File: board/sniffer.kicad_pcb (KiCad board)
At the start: 8 copper layers, 154 x 125 mm, 307 parts, among them J1 BARREL, J10 CONN_SFP_HOST, J11 SFP_CAGE, J12 PMOD_HOST, J13 CONN_SATA_DEVICE, J14 CONN_SATA_HOST, J15 CONN_LVDS_EXPANSION_HOST, J2 32K243-40ML5, J3 BEL_FUSE_0826-1G1T-23-F, J4 XILINX_JTAG, J5 32K243-40ML5, J6 32K243-40ML5, J7 32K243-40ML5, J8 CONN_SFF8087, J9 CONN_SFF8087, M1 SCREW_HOLE, M2 SCREW_HOLE, M3 SCREW_HOLE, M4 SCREW_HOLE, Q1 SSM6N58NU, U1 OKL-T_3-W12P-C, U10 KSZ9031RN, U11 74AVCH1T45, U12 74AVCH1T45, U13 74AVCH1T45, U14 74AVCH1T45, U15 W25Q128JV, U16 FPF2498, U17 FPF2498, U18 LP2996A, U2 LTC3374-QFN, U3 MYTNA1R84RELA2RA, U4 DDR3_SODIMM, U5 XC7K70T-2FBG484, U6 ECX2-LMV-7CN-156.250-TR, U7 ECX2-LMV-3CN-125.000-TR, U8 ECX2-LMV-3CN-125.000-TR, U9 SIT1602BC-72-18S-25.000000

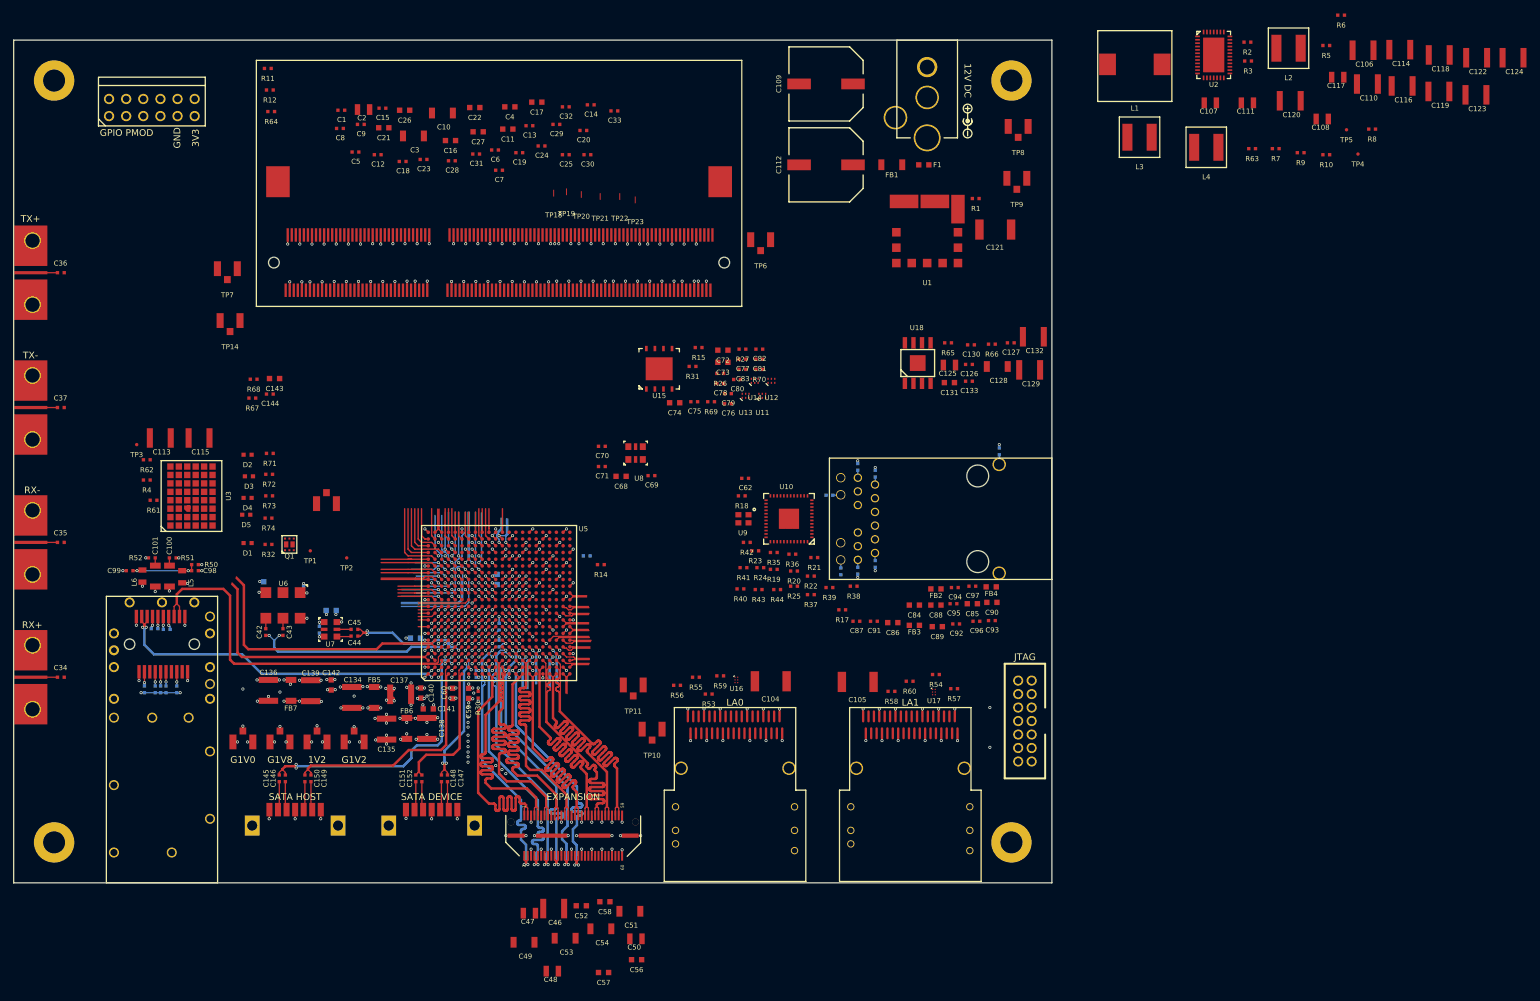
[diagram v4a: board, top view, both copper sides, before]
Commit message: Finished routing of south area of board including low speed SFP+ and LA connections. Started work on Ethernet.
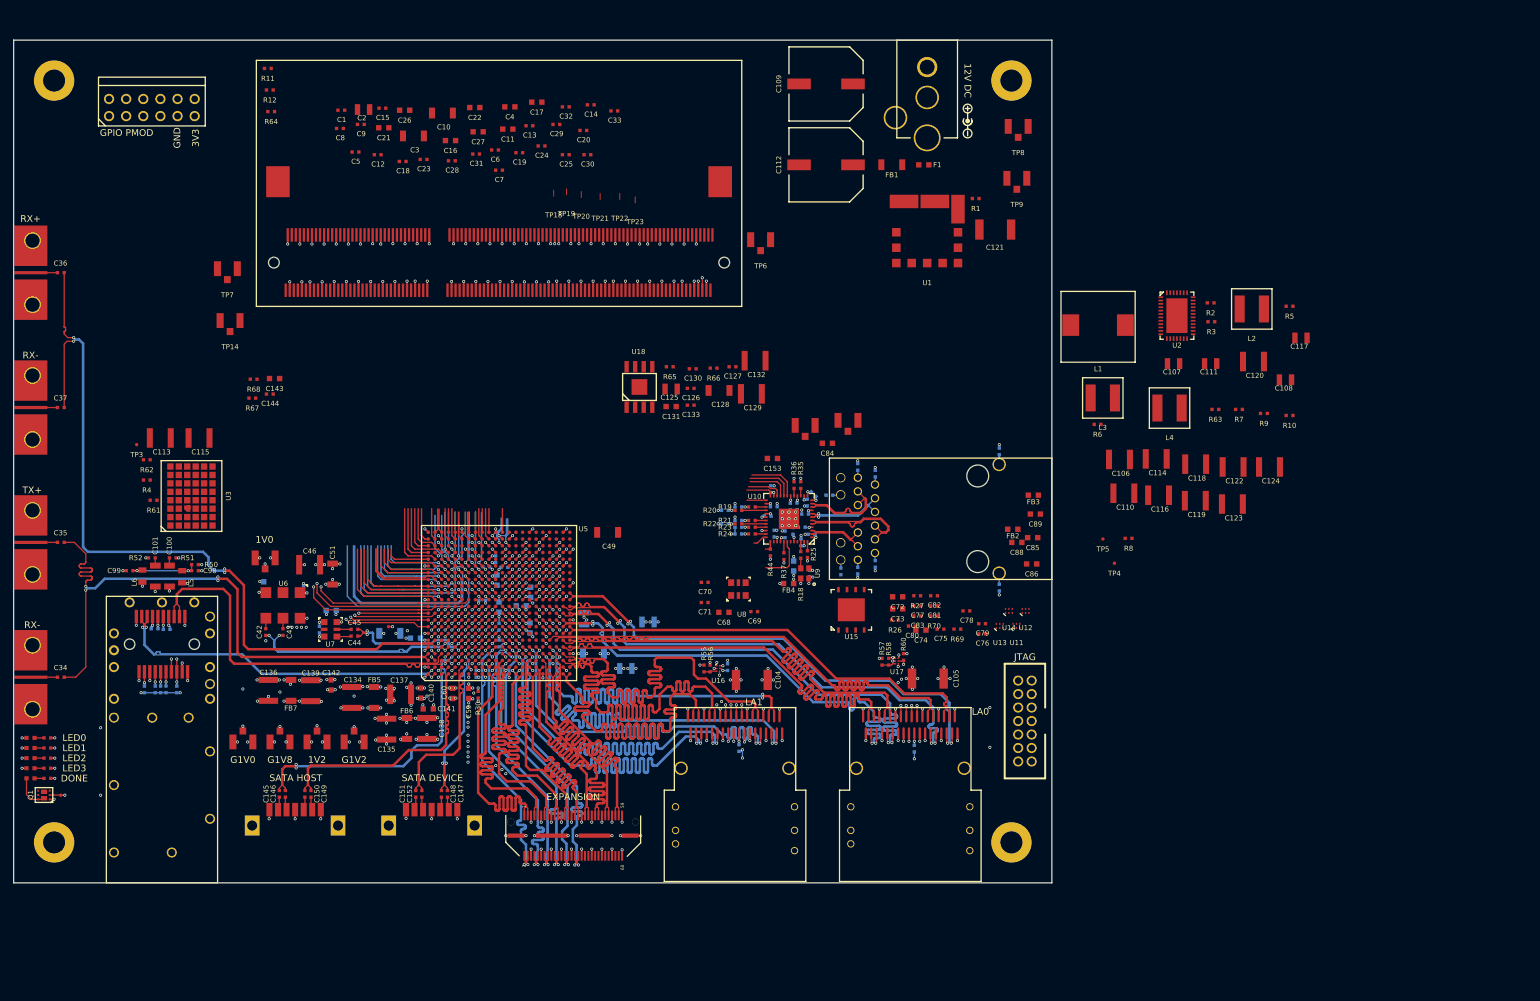
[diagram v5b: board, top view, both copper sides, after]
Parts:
- added C153: 4.7 uF, azonenberg_pcb:EIA_0603_CAP_NOSILK, F.Cu at (149.6, 95.0)
- added C154: 0.47 uF, azonenberg_pcb:EIA_0402_CAP_NOSILK, B.Cu at (152.2, 102.2)
- added C155: 0.47 uF, azonenberg_pcb:EIA_0402_CAP_NOSILK, B.Cu at (148.8, 103.6)
- added C156: 0.47 uF, azonenberg_pcb:EIA_0402_CAP_NOSILK, B.Cu at (154.7, 101.6)
- added C157: 0.47 uF, azonenberg_pcb:EIA_0402_CAP_NOSILK, B.Cu at (149.8, 102.2)
- added C158: 0.47 uF, azonenberg_pcb:EIA_0402_CAP_NOSILK, B.Cu at (149.8, 106.2)
- added C159: 0.47 uF, azonenberg_pcb:EIA_0402_CAP_NOSILK, B.Cu at (149.3, 99.6)
- C47, C48, C50, C52, C53, C54, C56, C57, C58, C62, C87, C90, C91, C92, C93, C94, C95, C96, C97, R14, R15, R17, R31, R38, R39, R40, R41, R42, R43, R53, R54, R59: moved to B.Cu
- U9: value SIT1602BC-72-18S-25.000000 -> ECS-2016MVQ-250-CN
- moved C110 70.6 mm to (201.7, 100.2)
- moved R6 70.6 mm to (197.8, 90.0)
- moved R8 70.6 mm to (202.4, 106.9)
- moved TP5 70.6 mm to (198.6, 107.0)
- moved C106 70.6 mm to (201.0, 95.2)
- moved C114 70.6 mm to (206.5, 95.1)
- moved C116 70.6 mm to (206.8, 100.5)
- moved C118 70.6 mm to (212.3, 95.9)
- moved C119 70.6 mm to (212.3, 101.3)
- moved C122 70.6 mm to (217.9, 96.3)
- moved C123 70.6 mm to (217.8, 101.8)
- moved TP4 70.6 mm to (200.3, 110.6)
- moved C124 70.6 mm to (223.3, 96.3)
- moved C51 66.7 mm to (84.3, 112.2), turned to 90 degrees
- moved C46 62.5 mm to (80.9, 110.8)
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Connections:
- C104 pad 1: /3.3V I/O/LA0_12V0 -> /3.3V I/O/LA1_12V0
- C105 pad 1: /3.3V I/O/LA1_12V0 -> /3.3V I/O/LA0_12V0
- C34 pad 1: /SERDES interfaces/GTX_TX3_P -> /SERDES interfaces/GTX_TX3_N
- C34 pad 2: /SERDES interfaces/GTX_TX3_AC_P -> /SERDES interfaces/GTX_TX3_AC_N
- C35 pad 1: /SERDES interfaces/GTX_TX3_N -> /SERDES interfaces/GTX_TX3_P
- C35 pad 2: /SERDES interfaces/GTX_TX3_AC_N -> /SERDES interfaces/GTX_TX3_AC_P
- C62 pad 1: /3V3 -> /1V8
- J6 pad 1: /SERDES interfaces/GTX_TX3_AC_P -> /SERDES interfaces/GTX_TX3_AC_N
- J7 pad 1: /SERDES interfaces/GTX_TX3_AC_N -> /SERDES interfaces/GTX_TX3_AC_P
- J8 pad A10: /3.3V I/O/LA0_PRESENCE_DETECT -> /3.3V I/O/LA1_PRESENCE_DETECT
- J8 pad A11: /3.3V I/O/LA0_12V0 -> /3.3V I/O/LA1_12V0
- J8 pad A13: /RGMII PHY/LA0_DQ6_P -> /Expansion connector/LA1_DQ6_P
- J8 pad A14: /RGMII PHY/LA0_DQ6_N -> /Expansion connector/LA1_DQ6_N
- J8 pad A16: /RGMII PHY/LA0_DQ7_P -> /Expansion connector/LA1_DQ7_P
- J8 pad A17: /RGMII PHY/LA0_DQ7_N -> /Expansion connector/LA1_DQ7_N
- J8 pad A2: /RGMII PHY/LA0_DQ4_P -> /Expansion connector/LA1_DQ4_P
- J8 pad A3: /RGMII PHY/LA0_DQ4_N -> /Expansion connector/LA1_DQ4_N
- J8 pad A5: /RGMII PHY/LA0_DQ5_P -> /Expansion connector/LA1_DQ5_P
- J8 pad A6: /RGMII PHY/LA0_DQ5_N -> /Expansion connector/LA1_DQ5_N
- J8 pad A8: /3.3V I/O/LA0_UART_RX -> /3.3V I/O/LA1_UART_RX
- J8 pad A9: /3.3V I/O/LA0_UART_TX -> /3.3V I/O/LA1_UART_TX
- J8 pad B10: /3.3V I/O/LA0_12V0 -> /3.3V I/O/LA1_12V0
- J8 pad B11: /3.3V I/O/LA0_12V0 -> /3.3V I/O/LA1_12V0
- J8 pad B13: /RGMII PHY/LA0_DQ2_P -> /Expansion connector/LA1_DQ2_P
- J8 pad B14: /RGMII PHY/LA0_DQ2_N -> /Expansion connector/LA1_DQ2_N
- J8 pad B16: /RGMII PHY/LA0_DQ3_P -> /Expansion connector/LA1_DQ3_P
- J8 pad B17: /RGMII PHY/LA0_DQ3_N -> /Expansion connector/LA1_DQ3_N
- J8 pad B2: /RGMII PHY/LA0_DQ0_P -> /Expansion connector/LA1_DQ0_P
- J8 pad B3: /RGMII PHY/LA0_DQ0_N -> /Expansion connector/LA1_DQ0_N
- J8 pad B5: /RGMII PHY/LA0_DQ1_P -> /Expansion connector/LA1_DQ1_P
- J8 pad B6: /RGMII PHY/LA0_DQ1_N -> /Expansion connector/LA1_DQ1_N
- J8 pad B8: /3.3V I/O/LA0_12V0 -> /3.3V I/O/LA1_12V0
- J8 pad B9: /3.3V I/O/LA0_12V0 -> /3.3V I/O/LA1_12V0
- J9 pad A10: /3.3V I/O/LA1_PRESENCE_DETECT -> /3.3V I/O/LA0_PRESENCE_DETECT
- J9 pad A11: /3.3V I/O/LA1_12V0 -> /3.3V I/O/LA0_12V0
- J9 pad A13: /Expansion connector/LA1_DQ6_P -> /RGMII PHY/LA0_DQ6_P
- J9 pad A14: /Expansion connector/LA1_DQ6_N -> /RGMII PHY/LA0_DQ6_N
- J9 pad A16: /Expansion connector/LA1_DQ7_P -> /RGMII PHY/LA0_DQ7_P
- J9 pad A17: /Expansion connector/LA1_DQ7_N -> /RGMII PHY/LA0_DQ7_N
- J9 pad A2: /Expansion connector/LA1_DQ4_P -> /RGMII PHY/LA0_DQ4_P
- J9 pad A3: /Expansion connector/LA1_DQ4_N -> /RGMII PHY/LA0_DQ4_N
- J9 pad A5: /Expansion connector/LA1_DQ5_P -> /RGMII PHY/LA0_DQ5_P
- J9 pad A6: /Expansion connector/LA1_DQ5_N -> /RGMII PHY/LA0_DQ5_N
- J9 pad A8: /3.3V I/O/LA1_UART_RX -> /3.3V I/O/LA0_UART_RX
- J9 pad A9: /3.3V I/O/LA1_UART_TX -> /3.3V I/O/LA0_UART_TX
- J9 pad B10: /3.3V I/O/LA1_12V0 -> /3.3V I/O/LA0_12V0
- J9 pad B11: /3.3V I/O/LA1_12V0 -> /3.3V I/O/LA0_12V0
- J9 pad B13: /Expansion connector/LA1_DQ2_P -> /RGMII PHY/LA0_DQ2_P
- J9 pad B14: /Expansion connector/LA1_DQ2_N -> /RGMII PHY/LA0_DQ2_N
- J9 pad B16: /Expansion connector/LA1_DQ3_P -> /RGMII PHY/LA0_DQ3_P
- J9 pad B17: /Expansion connector/LA1_DQ3_N -> /RGMII PHY/LA0_DQ3_N
- J9 pad B2: /Expansion connector/LA1_DQ0_P -> /RGMII PHY/LA0_DQ0_P
- J9 pad B3: /Expansion connector/LA1_DQ0_N -> /RGMII PHY/LA0_DQ0_N
- J9 pad B5: /Expansion connector/LA1_DQ1_P -> /RGMII PHY/LA0_DQ1_P
- J9 pad B6: /Expansion connector/LA1_DQ1_N -> /RGMII PHY/LA0_DQ1_N
- J9 pad B8: /3.3V I/O/LA1_12V0 -> /3.3V I/O/LA0_12V0
- J9 pad B9: /3.3V I/O/LA1_12V0 -> /3.3V I/O/LA0_12V0
- R53 pad 1: /3.3V I/O/LA0_PRESENCE_DETECT -> /3.3V I/O/LA1_PRESENCE_DETECT
- R54 pad 1: /3.3V I/O/LA1_PRESENCE_DETECT -> /3.3V I/O/LA0_PRESENCE_DETECT
- R59 pad 2: /3.3V I/O/LA0_12V0_EN -> /3.3V I/O/LA1_12V0_EN
- R60 pad 2: /3.3V I/O/LA1_12V0_EN -> /3.3V I/O/LA0_12V0_EN
- U16 pad B1: /3.3V I/O/LA0_12V0 -> /3.3V I/O/LA1_12V0
- U16 pad B2: /3.3V I/O/LA0_12V0_EN -> /3.3V I/O/LA1_12V0_EN
- U16 pad C2: /3.3V I/O/LA0_12V0_FAULT -> /3.3V I/O/LA1_12V0_FAULT
- U17 pad B1: /3.3V I/O/LA1_12V0 -> /3.3V I/O/LA0_12V0
- U17 pad B2: /3.3V I/O/LA1_12V0_EN -> /3.3V I/O/LA0_12V0_EN
- U17 pad C2: /3.3V I/O/LA1_12V0_FAULT -> /3.3V I/O/LA0_12V0_FAULT
- U5 pad A10: /3.3V I/O/ETH_LED1_P -> /3.3V I/O/LED3
- U5 pad A11: /3.3V I/O/PMOD_DQ1 -> /3.3V I/O/PMOD_DQ3
- U5 pad A9: /3.3V I/O/LED3 -> /3.3V I/O/LED1
- U5 pad AA1: /Expansion connector/LA1_DQ5_P -> /Expansion connector/LA1_DQ0_P
- U5 pad AA10: /RGMII PHY/LA0_DQ7_P -> /RGMII PHY/LA0_DQ5_P
- U5 pad AA11: /RGMII PHY/LA0_DQ2_P -> /RGMII PHY/LA0_DQ6_P
- U5 pad AA3: /Expansion connector/LA1_DQ6_P -> /Expansion connector/LA1_DQ1_N
- U5 pad AA4: /Expansion connector/LA1_DQ7_P -> /Expansion connector/LA1_DQ2_N
- U5 pad AA5: /RGMII PHY/LA0_DQ3_P -> /RGMII PHY/LA0_DQ0_P
- U5 pad AA6: /RGMII PHY/LA0_DQ4_P -> /RGMII PHY/LA0_DQ1_P
- U5 pad AA8: /RGMII PHY/LA0_DQ0_N -> /RGMII PHY/LA0_DQ4_P
- U5 pad AA9: /RGMII PHY/LA0_DQ0_P -> /RGMII PHY/LA0_DQ4_N
- U5 pad AB1: /Expansion connector/LA1_DQ5_N -> /Expansion connector/LA1_DQ0_N
- U5 pad AB10: /RGMII PHY/LA0_DQ7_N -> /RGMII PHY/LA0_DQ5_N
- U5 pad AB11: /RGMII PHY/LA0_DQ2_N -> /RGMII PHY/LA0_DQ6_N
- U5 pad AB12: /RGMII PHY/LA0_DQ1_N -> /RGMII PHY/LA0_DQ7_P
- U5 pad AB13: /RGMII PHY/LA0_DQ1_P -> /RGMII PHY/LA0_DQ7_N
- U5 pad AB2: /Expansion connector/LA1_DQ6_N -> /Expansion connector/LA1_DQ1_P
- U5 pad AB3: /Expansion connector/LA1_DQ7_N -> /Expansion connector/LA1_DQ2_P
- U5 pad AB5: /RGMII PHY/LA0_DQ3_N -> /RGMII PHY/LA0_DQ0_N
- U5 pad AB6: /RGMII PHY/LA0_DQ4_N -> /RGMII PHY/LA0_DQ1_N
- U5 pad AB7: /RGMII PHY/LA0_DQ5_N -> /RGMII PHY/LA0_DQ3_P
- U5 pad AB8: /RGMII PHY/LA0_DQ5_P -> /RGMII PHY/LA0_DQ3_N
- U5 pad B10: /3.3V I/O/PMOD_DQ7 -> /3.3V I/O/LED2
- U5 pad B11: /3.3V I/O/LED1 -> /3.3V I/O/PMOD_DQ6
- U5 pad B8: /3.3V I/O/LA1_12V0_FAULT -> /3.3V I/O/LA1_UART_RX
- U5 pad C10: /3.3V I/O/LA1_PRESENCE_DETECT -> /3.3V I/O/LA1_UART_TX
- U5 pad C8: /3.3V I/O/LA1_UART_TX -> /3.3V I/O/LA1_PRESENCE_DETECT
- U5 pad C9: /3.3V I/O/LA0_12V0_EN -> /3.3V I/O/LA1_12V0_EN
- U5 pad D10: /3.3V I/O/PMOD_DQ2 -> /3.3V I/O/PMOD_DQ5
- U5 pad D9: /3.3V I/O/LA1_12V0_EN -> /3.3V I/O/LA1_12V0_FAULT
- U5 pad E11: /3.3V I/O/SFP_TX_DISABLE -> /3.3V I/O/SFP_RX_LOS
- U5 pad E12: /3.3V I/O/SFP_TX_FAULT -> /3.3V I/O/SFP_MOD_ABS
- U5 pad E13: /SERDES interfaces/SFP_I2C_SCL -> /3.3V I/O/SFP_TX_DISABLE
- U5 pad E8: /3.3V I/O/LA1_UART_RX -> /3.3V I/O/LA0_UART_TX
- U5 pad E9: /3.3V I/O/LA0_12V0_FAULT -> /3.3V I/O/LA0_UART_RX
- U5 pad F10: /3.3V I/O/PMOD_DQ0 -> /3.3V I/O/PMOD_DQ1
- U5 pad F11: /3.3V I/O/SFP_RX_LOS -> /3.3V I/O/SFP_RS0
- U5 pad F13: /SERDES interfaces/SFP_I2C_SDA -> /3.3V I/O/SFP_TX_FAULT
- U5 pad F8: /3.3V I/O/LA0_UART_RX -> /3.3V I/O/LA0_12V0_EN
- U5 pad F9: /3.3V I/O/LA0_UART_TX -> /3.3V I/O/LA0_PRESENCE_DETECT
- U5 pad G11: /3.3V I/O/PMOD_DQ3 -> /3.3V I/O/PMOD_DQ2
- U5 pad G12: /3.3V I/O/PMOD_DQ6 -> /3.3V I/O/PMOD_DQ7
- U5 pad G13: /3.3V I/O/SFP_MOD_ABS -> /SERDES interfaces/SFP_I2C_SDA
- U5 pad G8: /3.3V I/O/LA0_PRESENCE_DETECT -> /3.3V I/O/LA0_12V0_FAULT
- U5 pad H10: /3.3V I/O/LED2 -> /3.3V I/O/PMOD_DQ0
- U5 pad H12: /3.3V I/O/PMOD_DQ5 -> (no net)
- U5 pad H13: /3.3V I/O/SFP_RS0 -> /SERDES interfaces/SFP_I2C_SCL
- U5 pad H8: (no net) -> /3.3V I/O/ETH_LED1_P
- U5 pad T13: /RGMII PHY/ETH_LED2_N_1V8 -> (no net)
- U5 pad T4: /Expansion connector/LA1_DQ3_P -> /Expansion connector/LA1_DQ5_P
- U5 pad T5: /Expansion connector/LA1_DQ1_P -> /Expansion connector/LA1_DQ6_P
- U5 pad T8: /RGMII PHY/RGMII_TX_CLK -> (no net)
- U5 pad T9: /RGMII PHY/RGMII_TXD3 -> (no net)
- U5 pad U3: /Expansion connector/LA1_DQ3_N -> /Expansion connector/LA1_DQ5_N
- U5 pad U5: /Expansion connector/LA1_DQ1_N -> /Expansion connector/LA1_DQ6_N
- U5 pad V4: /Expansion connector/LA1_DQ0_P -> /Expansion connector/LA1_DQ7_P
- U5 pad V7: (no net) -> /RGMII PHY/RGMII_TX_CLK
- U5 pad V8: (no net) -> /RGMII PHY/RGMII_TXD3
- U5 pad W10: (no net) -> /RGMII PHY/ETH_LED2_N_1V8
- U5 pad W4: /Expansion connector/LA1_DQ0_N -> /Expansion connector/LA1_DQ7_N
- U5 pad W5: /Expansion connector/LA1_DQ2_P -> /Expansion connector/LA1_DQ3_P
- U5 pad W6: /RGMII PHY/LA0_DQ6_P -> /RGMII PHY/LA0_DQ2_N
- U5 pad Y4: /Expansion connector/LA1_DQ2_N -> /Expansion connector/LA1_DQ3_N
- U5 pad Y6: /RGMII PHY/LA0_DQ6_N -> /RGMII PHY/LA0_DQ2_P
- U9 pad 1: /3V3 -> /1V8
- U9 pad 4: /3V3 -> /1V8
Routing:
- net /3V3: track 176.0 -> 465.0 mm, vias 13 -> 19
- net /12V0: track 0.00 -> 264.5 mm, vias 0 -> 4
- net /GND: track 1644.0 -> 1850.2 mm, vias 260 -> 318
- net /1V8: track 137.3 -> 292.1 mm, vias 31 -> 48
- net /3.3V I/O/PMOD_DQ4: track 0.71 -> 118.3 mm, vias 1 -> 2
- net /3.3V I/O/PMOD_DQ0: track 0.71 -> 118.2 mm, vias 1 -> 2
- net /3.3V I/O/PMOD_DQ5: track 0.71 -> 112.7 mm, vias 1 -> 2
- net /3.3V I/O/PMOD_DQ1: track 1.50 -> 112.7 mm, vias 0 -> 2
- net /3.3V I/O/PMOD_DQ2: track 0.71 -> 111.4 mm, vias 1 -> 2
- net /3.3V I/O/PMOD_DQ7: track 2.71 -> 108.4 mm, vias 0 -> 1
- net /3.3V I/O/PMOD_DQ3: track 0.71 -> 99.4 mm
- net /3.3V I/O/PMOD_DQ6: track 7.71 -> 104.6 mm, vias 0 -> 1
- net /FPGA support/FPGA_DONE: track 16.2 -> 91.1 mm, vias 1 -> 5
- net /3.3V I/O/LED2: track 0.71 -> 74.0 mm, vias 1 -> 2
- net /3.3V I/O/LED3: track 1.50 -> 73.9 mm, vias 0 -> 2
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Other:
- board text added: "1V0"
- board text added: "DONE"
- board text added: "LED0"
- board text added: "LED1"
- board text added: "LED2"
- board text added: "LED3"
- board text removed: "TX-"

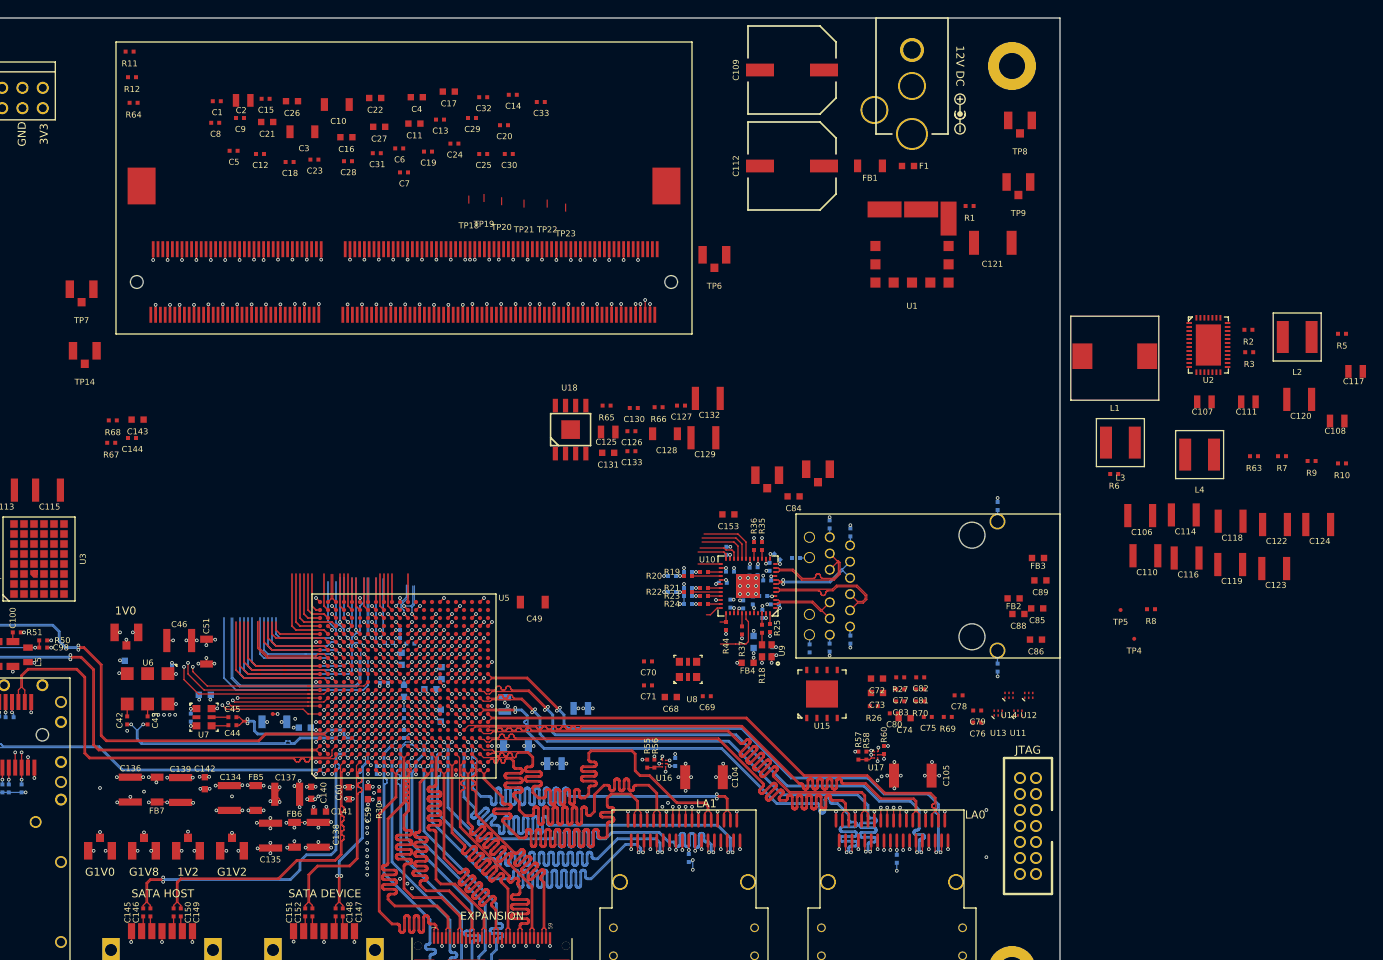
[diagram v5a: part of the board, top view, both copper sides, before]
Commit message: Finished routing almost everything except DDR.
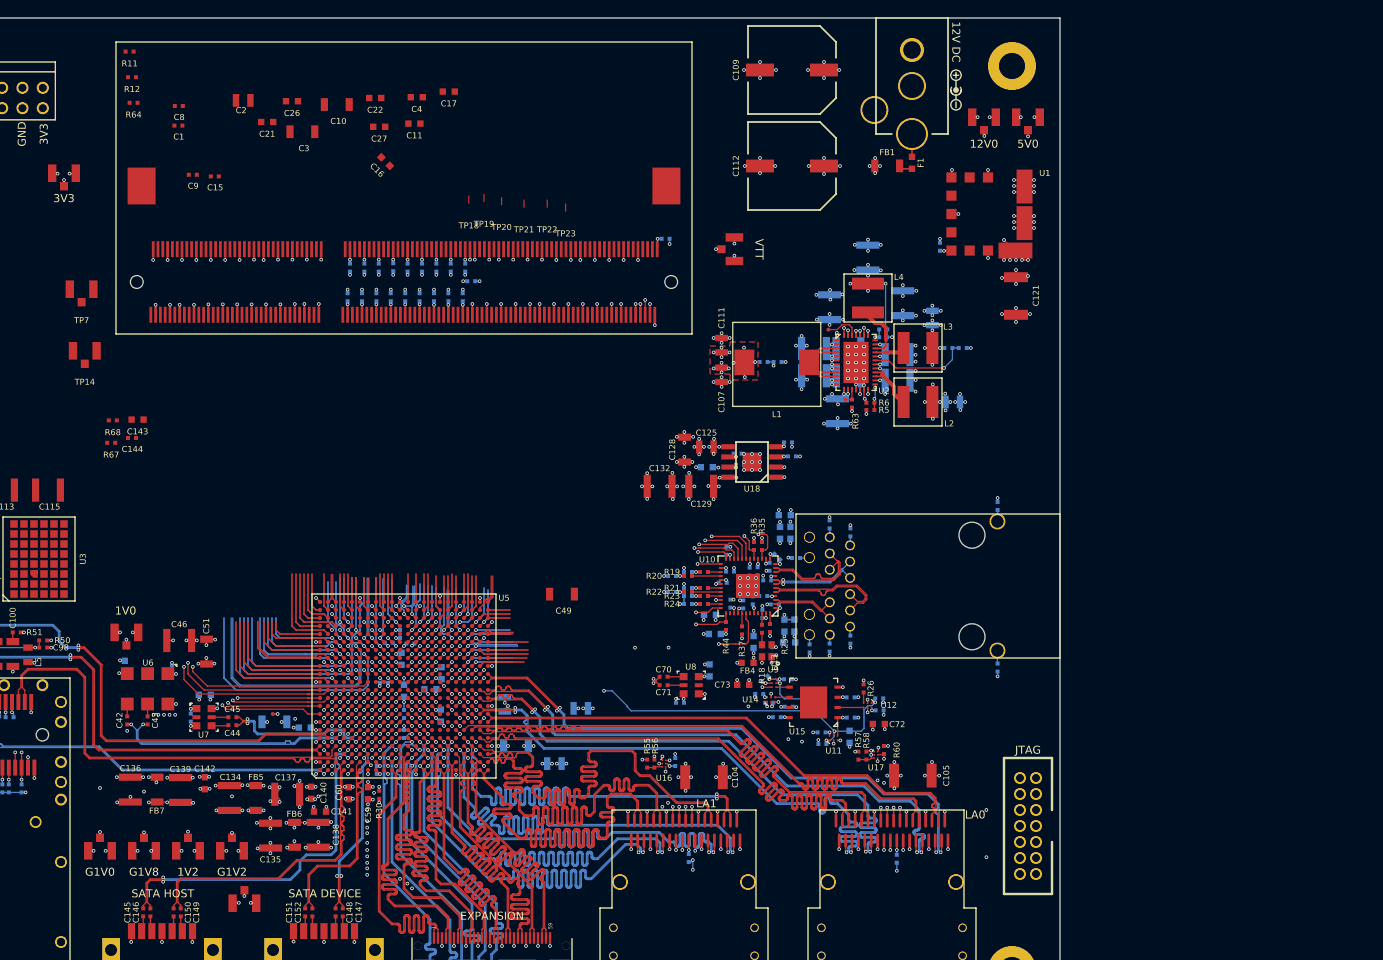
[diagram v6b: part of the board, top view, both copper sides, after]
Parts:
- C106, C108, C110, C114, C116, C117, C118, C119, C12, C120, C122, C123, C124, C126, C127, C13, C130, C131, C133, C14, C153, C18, C19, C20, C23, C24, C25, C28, C29, C30, C31, C32, C33, C5, C6, C68, C69, C7, C74, C75, C76, C77, C78, C79, C80, C81, C82, C83, C84, C85, C86, C88, C89, FB2, FB3, R1, R10, R2, R27, R3, R65, R66, R69, R7, R70, R8, R9: moved to B.Cu
- moved TP10 101.3 mm to (66.5, 52.5)
- moved TP11 84.3 mm to (89.0, 143.6), turned to 180 degrees
- moved C124 66.8 mm to (162.2, 69.2), turned to 90 degrees
- moved C111 66.2 mm to (148.7, 73.9), turned to 90 degrees
- moved R2 60.7 mm to (153.9, 76.0)
- moved C107 60.4 mm to (148.7, 77.6), turned to 270 degrees
- moved R5 59.7 mm to (167.3, 82.0)
- moved R10 59.5 mm to (168.9, 72.9)
- moved R3 59.0 mm to (155.7, 76.0)
- moved C123 58.0 mm to (163.2, 82.2), turned to 90 degrees
- moved C120 56.7 mm to (167.0, 63.0), turned to 90 degrees
- moved R9 56.0 mm to (168.9, 71.9), turned to 180 degrees
- moved TP4 54.4 mm to (162.1, 72.0)
- moved C117 53.3 mm to (175.1, 70.5), turned to 90 degrees
- moved C119 52.4 mm to (171.3, 68.7), turned to 90 degrees
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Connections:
- net Net-(R10-Pad1) renamed /Power Supply/3V3_FB
- net Net-(R7-Pad2) renamed /Power Supply/1V8_FB
- R5 pad 2: /Power Supply/1V35_FB -> /Power Supply/1V2_FB
- R6 pad 1: /Power Supply/1V35_FB -> /Power Supply/1V2_FB
- U2 pad 20: /Power Supply/1V35_FB -> /Power Supply/1V2_FB
- U5 pad AA13: /RGMII PHY/ETH_LED1_N_1V8 -> /RGMII PHY/RGMII_TXD0
- U5 pad H8: /3.3V I/O/ETH_LED1_P -> /3.3V I/O/ETH_LED2_P
- U5 pad H9: /3.3V I/O/ETH_LED2_P -> /3.3V I/O/ETH_LED1_P
- U5 pad U10: /RGMII PHY/CLK_125_AC_P -> /RGMII PHY/CLK_125_AC_N
- U5 pad U11: /RGMII PHY/ETH_RST_N -> /RGMII PHY/ETH_RXD3
- U5 pad U12: /RGMII PHY/ETH_MDC -> /RGMII PHY/ETH_LED1_N_1V8
- U5 pad U13: /RGMII PHY/ETH_MDIO -> /RGMII PHY/ETH_LED2_N_1V8
- U5 pad V12: /RGMII PHY/ETH_RXD0 -> /RGMII PHY/RGMII_TX_EN
- U5 pad V13: /RGMII PHY/ETH_RXD1 -> /RGMII PHY/RGMII_TXD2
- U5 pad V7: /RGMII PHY/RGMII_TX_CLK -> /RGMII PHY/ETH_RST_N
- U5 pad V8: /RGMII PHY/RGMII_TXD3 -> /RGMII PHY/ETH_MDC
- U5 pad V9: /RGMII PHY/CLK_125_AC_N -> /RGMII PHY/CLK_125_AC_P
- U5 pad W10: /RGMII PHY/ETH_LED2_N_1V8 -> /RGMII PHY/ETH_RXD1
- U5 pad W11: /RGMII PHY/ETH_RXD3 -> /RGMII PHY/ETH_RXD0
- U5 pad W12: /RGMII PHY/RGMII_TXD1 -> /RGMII PHY/RGMII_TX_CLK
- U5 pad W9: /RGMII PHY/RGMII_TXD0 -> /RGMII PHY/ETH_RX_CLK
- U5 pad Y12: /RGMII PHY/RGMII_TXD2 -> /RGMII PHY/RGMII_TXD3
- U5 pad Y13: /RGMII PHY/RGMII_TX_EN -> /RGMII PHY/RGMII_TXD1
- U5 pad Y8: /RGMII PHY/ETH_RX_CLK -> /RGMII PHY/ETH_MDIO
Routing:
- net /GND: track 1850.2 -> 2409.9 mm, vias 318 -> 484
- net /5V0: track 38.0 -> 351.8 mm, vias 2 -> 42
- net /3V3: track 465.0 -> 646.8 mm, vias 19 -> 44
- net /1V35: track 179.4 -> 352.0 mm, vias 36 -> 61
- net /1V2: track 94.9 -> 201.3 mm, vias 12 -> 24
- net /12V0: track 264.5 -> 359.8 mm, vias 4 -> 25
- net /RAM_VTT: track 0.00 -> 85.8 mm, vias 0 -> 12
- net /Boot flash/FLASH_SO: track 0.71 -> 80.5 mm, vias 1 -> 4
- net /1V8: track 292.1 -> 371.7 mm, vias 48 -> 59
- net /Boot flash/FLASH_CS: track 0.00 -> 70.8 mm, vias 0 -> 2
- net /3.3V I/O/ETH_LED1_P: track 17.8 -> 85.6 mm, vias 1 -> 3
- net /3.3V I/O/ETH_LED2_P: track 17.8 -> 75.2 mm, vias 1 -> 3
- net /RGMII PHY/ETH_LED2_N_1V8: track 1.10 -> 57.4 mm, vias 0 -> 2
- net /Power Supply/VDDQ_SENSE: track 0.00 -> 55.9 mm, vias 0 -> 5
- net /RGMII PHY/ETH_LED1_N_1V8: track 1.10 -> 55.1 mm, vias 0 -> 2
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- added copper zone on F.Cu, net /1V35
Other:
- board text added: "!!FIXME!!"
- board text added: "12V0"
- board text added: "5V0"
- board text added: "VTT"
